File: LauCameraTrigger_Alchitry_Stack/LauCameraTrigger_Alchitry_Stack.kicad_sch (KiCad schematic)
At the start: 17 parts, among them J1 DF40C-50DP (Site A / +3V3 onl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, J2 DF40C-80DP (Bank A / Site B /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, J3 DF40C-80DP (Bank B / Site C), J4 SM07B-SRSS-TB, J5 SM07B-SRSS-TB, J6 SM07B-SRSS-TB, SW1 DIP4 RGB/HV select

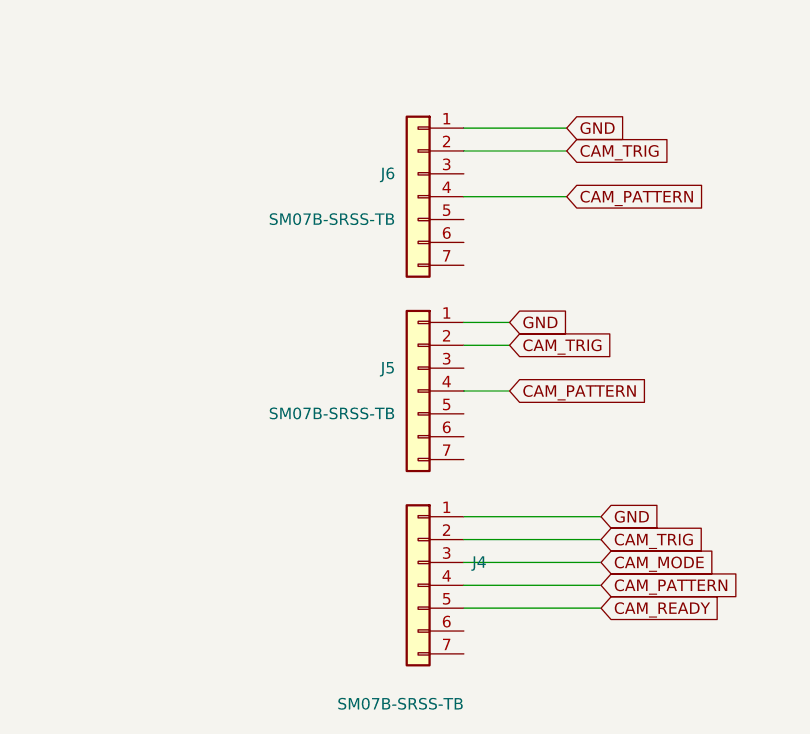
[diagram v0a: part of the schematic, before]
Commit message: LauCameraTrigger stacking board: unique JST refs + corrected order files
Rename the three JSTs to MASTER1/SLAVE1/SLAVE2 (resolving a duplicate SLAVE reference designator) so the assembly CPL has unique designators; PCB synced via F8. Regenerate production bom/bom_full/cpl from the corrected board with matched MPNs (DF40C-80DP/50DP-0.4V(51), SM07B-SRSS-TB). Matches the JLCPCB rev-1 PCBA order. FPGA Bank-B remap intentionally left uncommitted until the board is validated.

Co-Authored-By: Claude Opus 4.8 (1M context) <noreply@anthropic.com>
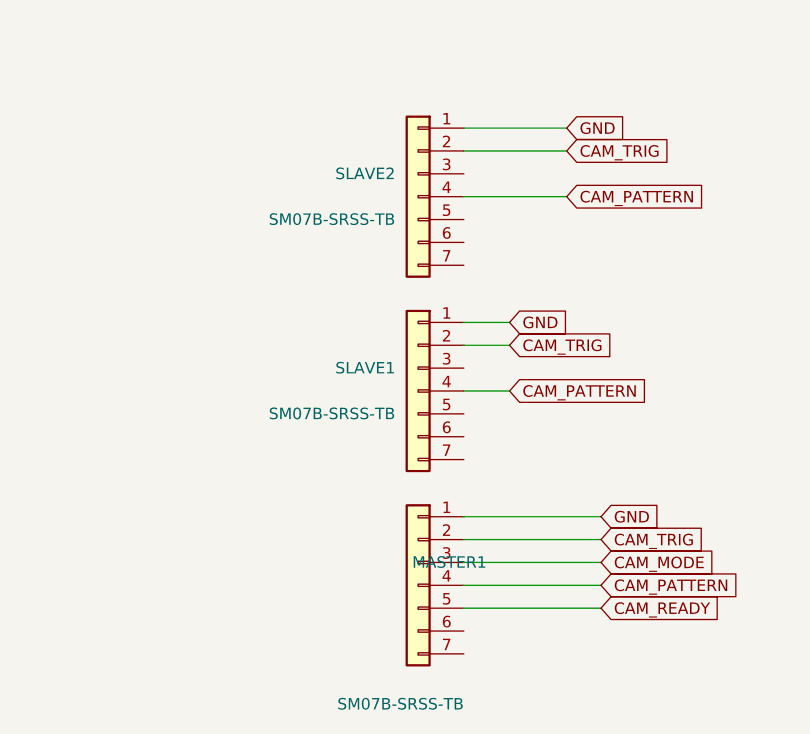
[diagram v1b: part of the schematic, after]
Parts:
- renumbered J4 to MASTER1, J5 to SLAVE1, J6 to SLAVE2
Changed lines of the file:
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@@
 	(global_label "GND"
 		(shape input)
+		(at 292.62 182.54 0)
+		(effects
+			(font
+				(size 1.27 1.27)
+			)
+			(justify left)
+		)
+		(property "Intersheetrefs" "${INTERSHEET_REFS}"
+			(at 292.62 182.54 0)
+			(hide yes)
+			(show_name no)
+			(do_not_autoplace no)
+			(effects
+				(font
+					(size 1.27 1.27)
+				)
+			)
+		)
+	)
+	(global_label "GND"
+		(shape input)
 		(at 134.62 46.99 180)
 		(effects
@@
 		)
 	)
+	(global_label "SW_GREEN"
+		(shape input)
+		(at 277.38 180 0)
+		(effects
+			(font
+				(size 1.27 1.27)
+			)
+			(justify left)
+		)
+		(property "Intersheetrefs" "${INTERSHEET_REFS}"
+			(at 277.38 180 0)
+			(hide yes)
+			(show_name no)
+			(do_not_autoplace no)
+			(effects
+				(font
+					(size 1.27 1.27)
+				)
+			)
+		)
+	)
 	(global_label "CAM_PATTERN"
 		(shape input)
@@
 		)
 	)
+	(global_label "SW_BLUE"
+		(shape input)
+		(at 277.38 177.46 0)
+		(effects
+			(font
+				(size 1.27 1.27)
+			)
+			(justify left)
+		)
+		(property "Intersheetrefs" "${INTERSHEET_REFS}"
+			(at 277.38 177.46 0)
+			(hide yes)
+			(show_name no)
+			(do_not_autoplace no)
+			(effects
+				(font
+					(size 1.27 1.27)
+				)
+			)
+		)
+	)
 	(global_label "+3V3"
 		(shape input)
@@
 	(global_label "GND"
 		(shape input)
+		(at 292.62 180 0)
+		(effects
+			(font
+				(size 1.27 1.27)
+			)
+			(justify left)
+		)
+		(property "Intersheetrefs" "${INTERSHEET_REFS}"
+			(at 292.62 180 0)
+			(hide yes)
+			(show_name no)
+			(do_not_autoplace no)
+			(effects
+				(font
+					(size 1.27 1.27)
+				)
+			)
+		)
+	)
+	(global_label "GND"
+		(shape input)
 		(at 134.62 31.75 180)
 		(effects
@@
 		)
 	)
+	(global_label "+3V3"
+		(shape input)
+		(at 292.62 174.92 0)
+		(effects
+			(font
+				(size 1.27 1.27)
+			)
+			(justify left)
+		)
+		(property "Intersheetrefs" "${INTERSHEET_REFS}"
+			(at 292.62 174.92 0)
+			(hide yes)
+			(show_name no)
+			(do_not_autoplace no)
+			(effects
+				(font
+					(size 1.27 1.27)
+				)
+			)
+		)
+	)
+	(global_label "SW_RED"
+		(shape input)
+		(at 277.38 182.54 0)
+		(effects
+			(font
+				(size 1.27 1.27)
+			)
+			(justify left)
+		)
+		(property "Intersheetrefs" "${INTERSHEET_REFS}"
+			(at 277.38 182.54 0)
+			(hide yes)
+			(show_name no)
+			(do_not_autoplace no)
+			(effects
+				(font
+					(size 1.27 1.27)
+				)
+			)
+		)
+	)
 	(global_label "GND"
 		(shape input)
@@
 		)
 	)
+	(global_label "GND"
+		(shape input)
+		(at 292.62 177.46 0)
+		(effects
+			(font
+				(size 1.27 1.27)
+			)
+			(justify left)
+		)
+		(property "Intersheetrefs" "${INTERSHEET_REFS}"
+			(at 292.62 177.46 0)
+			(hide yes)
+			(show_name no)
+			(do_not_autoplace no)
+			(effects
+				(font
+					(size 1.27 1.27)
+				)
+			)
+		)
+	)
 	(global_label "CAM_TRIG"
 		(shape input)
@@
 		(property "Intersheetrefs" "${INTERSHEET_REFS}"
 			(at 347.98 112.53 0)
+			(hide yes)
+			(show_name no)
+			(do_not_autoplace no)
+			(effects
+				(font
+					(size 1.27 1.27)
+				)
+			)
+		)
+	)
+	(global_label "SW_HVSV"
+		(shape input)
+		(at 277.38 174.92 0)
+		(effects
+			(font
+				(size 1.27 1.27)
+			)
+			(justify left)
+		)
+		(property "Intersheetrefs" "${INTERSHEET_REFS}"
+			(at 277.38 174.92 0)
 			(hide yes)
 			(show_name no)
@@
 	)
 	(symbol
+		(lib_id "Switch:SW_DIP_x04")
+		(at 285 180 0)
+		(unit 1)
+		(body_style 1)
+		(exclude_from_sim no)
+		(in_bom yes)
+		(on_board yes)
+		(in_pos_files yes)
+		(dnp no)
+		(property "Reference" "SW1"
+			(at 286 168 0)
+			(show_name no)
+			(do_not_autoplace no)
+			(effects
+				(font
+					(size 1.27 1.27)
+				)
+				(justify left)
+			)
+		)
+		(property "Value" "DIP4 RGB/HV select"
+			(at 286 192 0)
+			(show_name no)
+			(do_not_autoplace no)
+			(effects
+				(font
+					(size 1.27 1.27)
+				)
+				(justify left)
+			)
+		)
+		(property "Footprint" "Button_Switch_SMD:SW_DIP_SPSTx04_Slide_6.7x11.72mm_W8.61mm_P2.54mm_LowProfile"
+			(at 285 180 0)
+			(hide yes)
+			(show_name no)
+			(do_not_autoplace no)
+			(effects
+				(font
+					(size 1.27 1.27)
+				)
+			)
+		)
+		(property "Datasheet" ""
+			(at 285 180 0)
+			(show_name no)
+			(do_not_autoplace no)
+			(effects
+				(font
+					(size 1.27 1.27)
+				)
+			)
+		)
+		(property "Description" ""
+			(at 285 180 0)
+			(show_name no)
+			(do_not_autoplace no)
+			(effects
+				(font
+					(size 1.27 1.27)
+				)
+			)
+		)
+		(pin "1"
+		)
+		(pin "2"
+		)
+		(pin "3"
+		)
+		(pin "4"
+		)
+		(pin "5"
+		)
+		(pin "6"
+		)
+		(pin "7"
+		)
+		(pin "8"
+		)
+		(instances
+			(project "LauCameraTrigger_Alchitry_Stack"
+				(path "/11111111-2222-3333-4444-555555555555"
+					(reference "SW1")
+					(unit 1)
+				)
+			)
+		)
+	)
+	(symbol
 		(lib_id "Connector_Generic:Conn_01x07")
 		(at 184.15 179.07 0)
@@
 		(in_pos_files yes)
 		(dnp no)
-		(property "Reference" "J6"
+		(property "Reference" "SLAVE2"
 			(at 181.61 176.53 0)
 			(show_name no)
@@
 			(project "LauCameraTrigger_Alchitry_Stack"
 				(path "/11111111-2222-3333-4444-555555555555"
-					(reference "J6")
+					(reference "SLAVE2")
 					(unit 1)
 				)
@@
 		(in_pos_files yes)
 		(dnp no)
-		(property "Reference" "J5"
+		(property "Reference" "SLAVE1"
 			(at 181.61 198.12 0)
 			(show_name no)
@@
 			(project "LauCameraTrigger_Alchitry_Stack"
 				(path "/11111111-2222-3333-4444-555555555555"
-					(reference "J5")
+					(reference "SLAVE1")
 					(unit 1)
 				)
@@
 		(in_pos_files yes)
 		(dnp no)
-		(property "Reference" "J4"
+		(property "Reference" "MASTER1"
 			(at 191.77 219.71 0)
 			(show_name no)
@@
 			(project "LauCameraTrigger_Alchitry_Stack"
 				(path "/11111111-2222-3333-4444-555555555555"
-					(reference "J4")
+					(reference "MASTER1")
 					(unit 1)
 				)
@@
 		)
 	)
-	(symbol
-		(lib_id "Switch:SW_DIP_x04")
-		(at 285 180 0)
-		(unit 1)
-		(exclude_from_sim no)
-		(in_bom yes)
-		(on_board yes)
-		(dnp no)
-		(property "Reference" "SW1"
-			(at 286 168 0)
-			(effects (font (size 1.27 1.27)) (justify left))
-		)
-		(property "Value" "DIP4 RGB/HV select"
-			(at 286 192 0)
-			(effects (font (size 1.27 1.27)) (justify left))
-		)
-		(property "Footprint" "Button_Switch_SMD:SW_DIP_SPSTx04_Slide_6.7x11.72mm_W8.61mm_P2.54mm_LowProfile"
-			(at 285 180 0)
-			(effects (font (size 1.27 1.27)) (hide yes))
-		)
-		(pin "1"
-		)
-		(pin "2"
-		)
-		(pin "3"
-		)
-		(pin "4"
-		)
-		(pin "5"
-		)
-		(pin "6"
-		)
-		(pin "7"
-		)
-		(pin "8"
-		)
-		(instances
-			(project "LauCameraTrigger_Alchitry_Stack"
-				(path "/11111111-2222-3333-4444-555555555555"
-					(reference "SW1")
-					(unit 1)
-				)
-			)
-		)
-	)
-	(global_label "SW_HVSV"
-		(shape input)
-		(at 277.38 174.92 0)
-		(effects (font (size 1.27 1.27)) (justify left))
-	)
-	(global_label "SW_BLUE"
-		(shape input)
-		(at 277.38 177.46 0)
-		(effects (font (size 1.27 1.27)) (justify left))
-	)
-	(global_label "SW_GREEN"
-		(shape input)
-		(at 277.38 180.0 0)
-		(effects (font (size 1.27 1.27)) (justify left))
-	)
-	(global_label "SW_RED"
-		(shape input)
-		(at 277.38 182.54 0)
-		(effects (font (size 1.27 1.27)) (justify left))
-	)
-	(global_label "+3V3"
-		(shape input)
-		(at 292.62 174.92 0)
-		(effects (font (size 1.27 1.27)) (justify left))
-	)
-	(global_label "GND"
-		(shape input)
-		(at 292.62 177.46 0)
-		(effects (font (size 1.27 1.27)) (justify left))
-	)
-	(global_label "GND"
-		(shape input)
-		(at 292.62 180.0 0)
-		(effects (font (size 1.27 1.27)) (justify left))
-	)
-	(global_label "GND"
-		(shape input)
-		(at 292.62 182.54 0)
-		(effects (font (size 1.27 1.27)) (justify left))
-	)
 	(sheet_instances

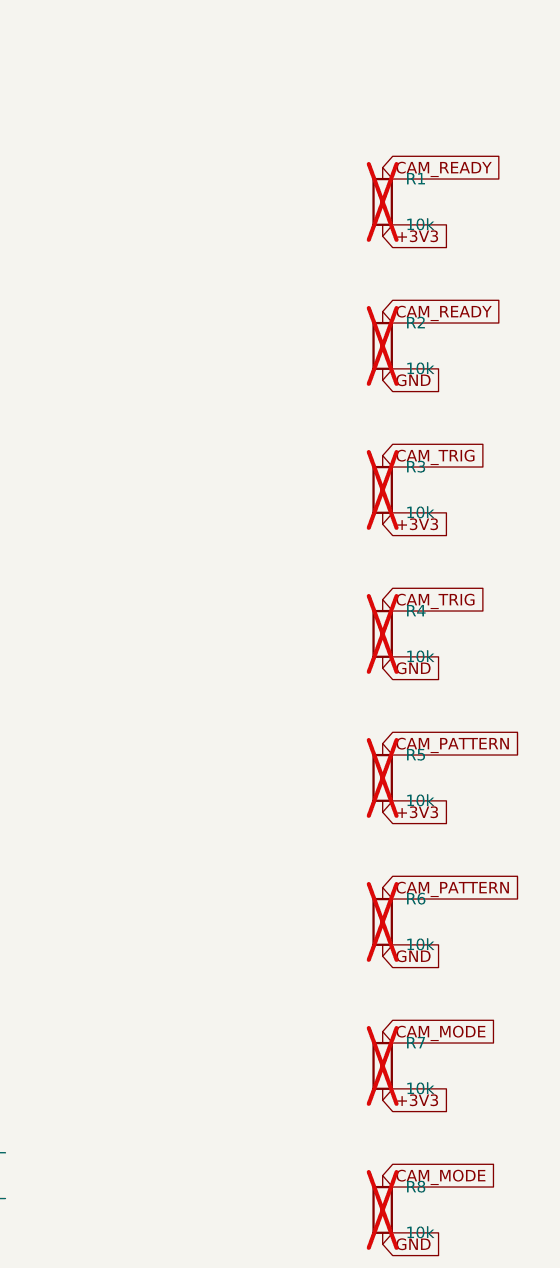
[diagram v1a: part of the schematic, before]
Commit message: hw: populate 1k tie-high pull-ups (R1/R7) + silkscreen relabel/branding
Camera-line pull-ups for a Basler ace: the ace signal outputs (opto Line 2
and direct-coupled GPIO) are open-collector, so CAM_READY (R1) and CAM_MODE
(R7) need an external pull-up to +3V3 to read a valid logic high. Populate
R1/R7 = 1k (JLCPCB C4410 / UNI-ROYAL 1206W4F1001T5E); leave the FPGA-driven
outputs (R3/R5) and all tie-low positions DNP. Updates bom.csv, cpl.csv,
bom_full.csv, PCB/sch source (value + un-DNP), and SCHEMATIC.md rationale.

Silkscreen: relabel camera connectors to SLAVE / MASTER / SLAVE (plain silk;
unique designators MASTER1/SLAVE1/SLAVE2 kept for BOM/placement). Add
https://drhalftone.com and author "Daniel L. Lau" on front silk plus a
title block (author in company field) on the PCB and schematic.

NOTE: silkscreen changed -> gerbers/gerbers.zip are stale and must be
re-plotted in KiCad before the next fab order.

Co-Authored-By: Claude Opus 4.8 (1M context) <noreply@anthropic.com>
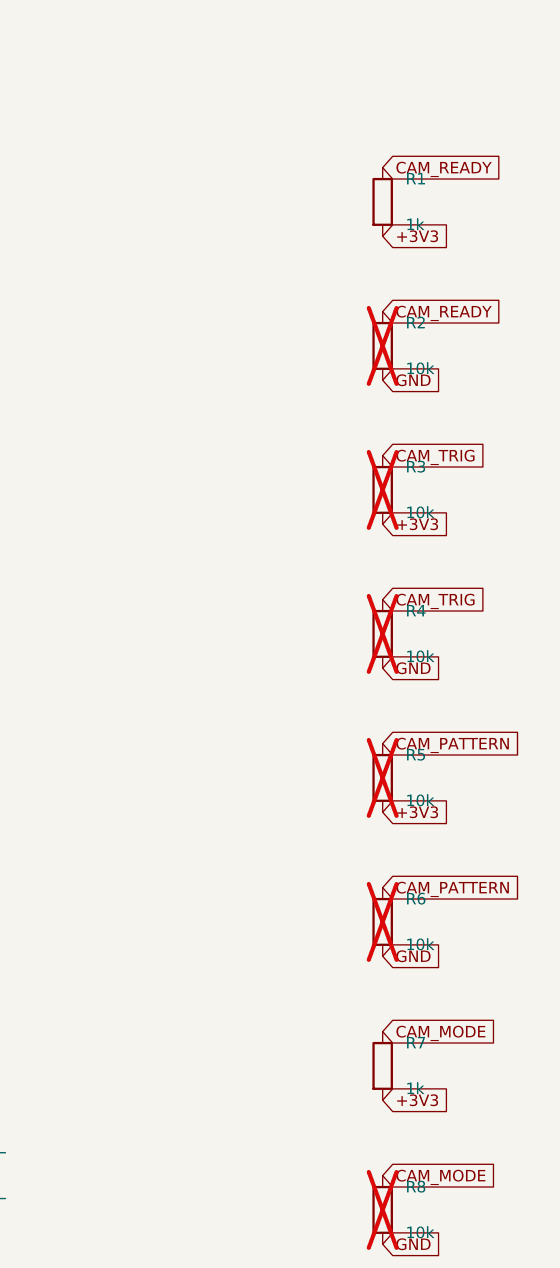
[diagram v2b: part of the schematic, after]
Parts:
- R1, R7: value 10k -> 1k; now fitted
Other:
- company: (none) -> Daniel L. Lau
- title: (none) -> LauCameraTrigger_Alchitry_Stack
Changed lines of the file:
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@@
 	(generator_version "10.0")
 	(paper "A3")
+	(title_block
+		(title "LauCameraTrigger_Alchitry_Stack")
+		(date "2026-07-02")
+		(company "Daniel L. Lau")
+		(comment 1 "https://drhalftone.com")
+	)
 	(wire
 		(pts
@@
 		(on_board yes)
 		(in_pos_files yes)
-		(dnp yes)
+		(dnp no)
 		(property "Reference" "R1"
 			(at 350.52 65.8 0)
@@
 			)
 		)
-		(property "Value" "10k"
+		(property "Value" "1k"
 			(at 350.52 70.88 0)
 			(show_name no)
@@
 		(on_board yes)
 		(in_pos_files yes)
-		(dnp yes)
+		(dnp no)
 		(property "Reference" "R7"
 			(at 350.52 161.8 0)
@@
 			)
 		)
-		(property "Value" "10k"
+		(property "Value" "1k"
 			(at 350.52 166.88 0)
 			(show_name no)
